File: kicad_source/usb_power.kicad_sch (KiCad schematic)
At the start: 38 parts, among them P1 USB_OTG, Q1 2N7002, Q2 2N7002, Q3 BC847, Q4 BC847, Q5 NTR4171P, SW3 SWITCH_INV, U1 TPS383X, U2 MCP73831, U3 TPS736XX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

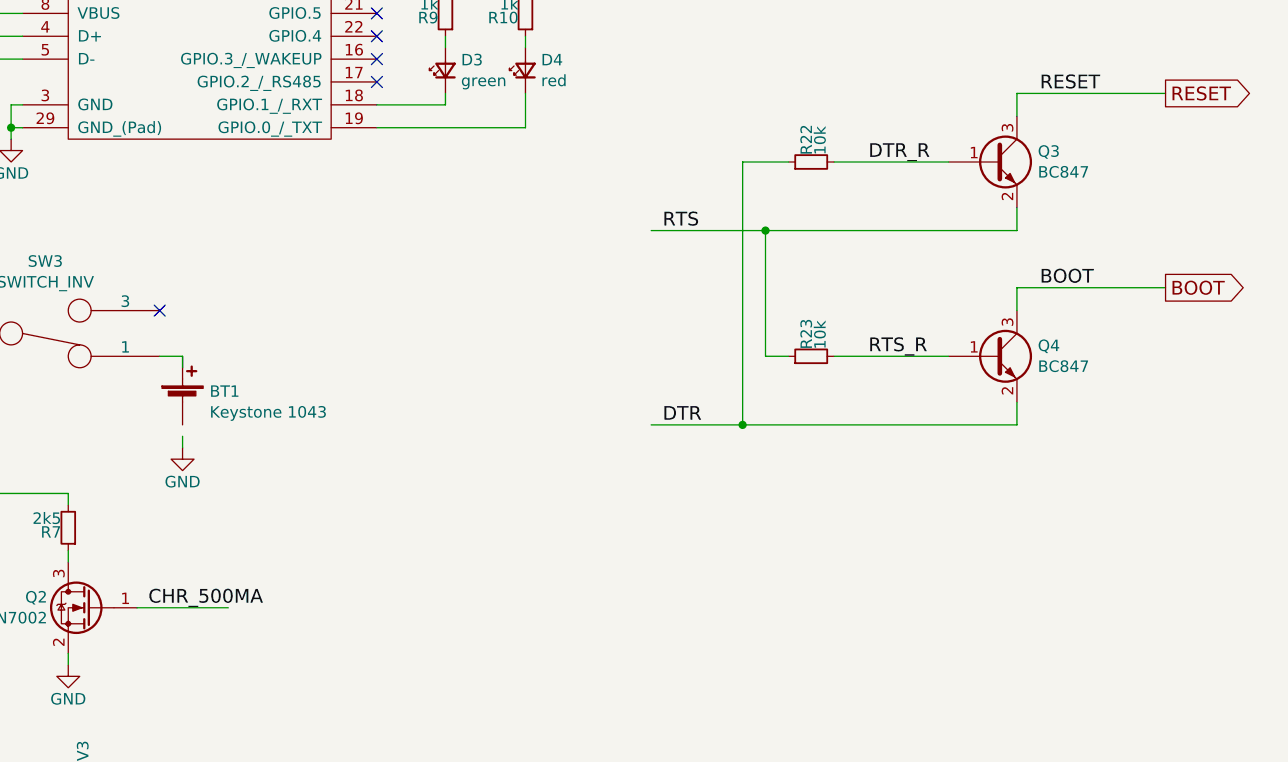
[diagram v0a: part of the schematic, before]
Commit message: added pull up on BOOT
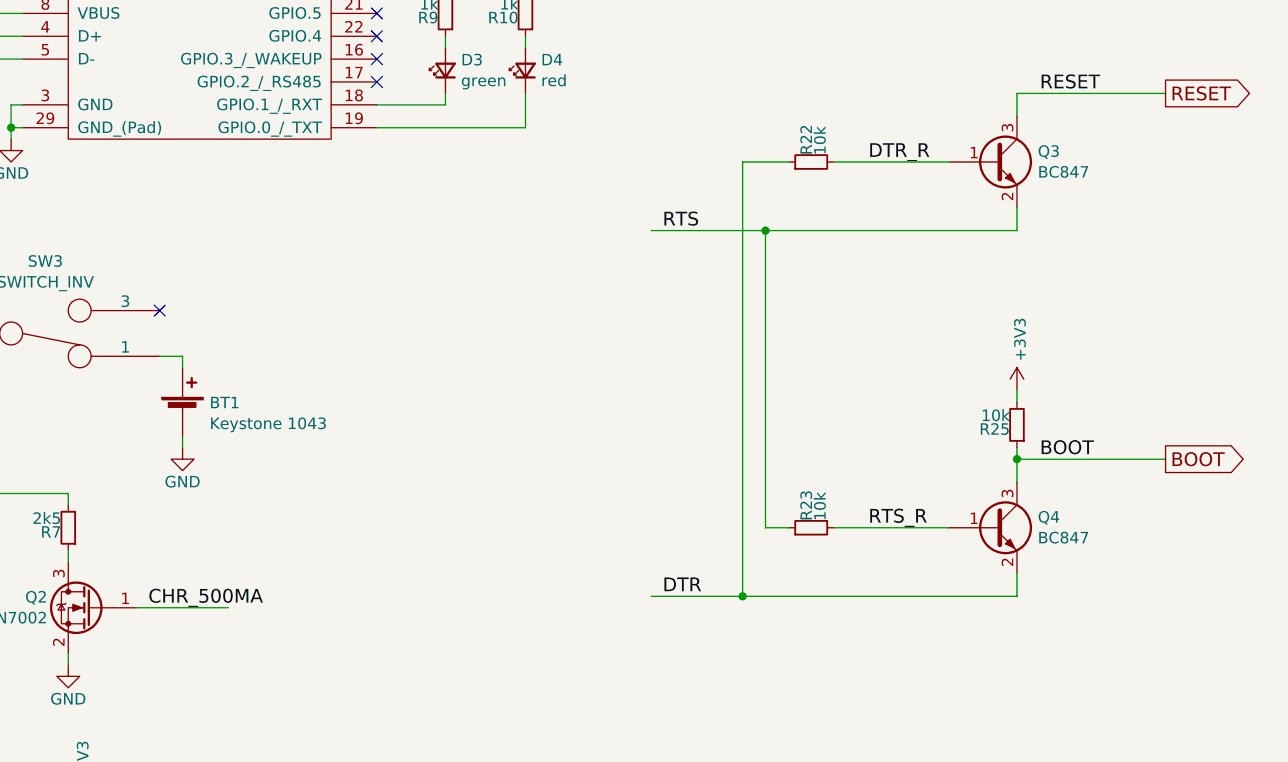
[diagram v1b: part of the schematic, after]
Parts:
- added R25: 10k, Resistor_SMD:R_0603_1608Metric, symbol Device:R_Small
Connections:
- net +3V3: now also R25.2
- net BOOT: now also R25.1
- net GND: now also BT1.2 (-)
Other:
- moved on the sheet: BT1, Q4, R23
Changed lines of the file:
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@@
   (junction (at 110.49 62.23) (diameter 0) (color 0 0 0 0)
   )
+  (junction (at 251.46 121.92) (diameter 0) (color 0 0 0 0)
+  )
   (junction (at 124.46 64.77) (diameter 0) (color 0 0 0 0)
   )
-  (junction (at 220.98 118.11) (diameter 0) (color 0 0 0 0)
+  (junction (at 220.98 137.16) (diameter 0) (color 0 0 0 0)
   )
   (junction (at 116.84 110.49) (diameter 0) (color 0 0 0 0)
@@
     (stroke (width 0) (type default) (color 0 0 0 0))
   )
-  (wire (pts (xy 220.98 118.11) (xy 220.98 88.9))
+  (wire (pts (xy 220.98 88.9) (xy 220.98 137.16))
     (stroke (width 0) (type default) (color 0 0 0 0))
   )
@@
     (stroke (width 0) (type default) (color 0 0 0 0))
   )
-  (wire (pts (xy 223.52 110.49) (xy 226.06 110.49))
+  (wire (pts (xy 223.52 129.54) (xy 226.06 129.54))
     (stroke (width 0) (type default) (color 0 0 0 0))
   )
@@
     (stroke (width 0) (type default) (color 0 0 0 0))
   )
-  (wire (pts (xy 251.46 102.87) (xy 251.46 105.41))
+  (wire (pts (xy 251.46 121.92) (xy 251.46 124.46))
     (stroke (width 0) (type default) (color 0 0 0 0))
   )
@@
     (stroke (width 0) (type default) (color 0 0 0 0))
   )
+  (wire (pts (xy 251.46 114.3) (xy 251.46 115.57))
+    (stroke (width 0) (type default) (color 0 0 0 0))
+  )
   (wire (pts (xy 127 54.61) (xy 140.97 54.61))
     (stroke (width 0) (type default) (color 0 0 0 0))
@@
     (stroke (width 0) (type default) (color 0 0 0 0))
   )
-  (wire (pts (xy 223.52 96.52) (xy 223.52 110.49))
-    (stroke (width 0) (type default) (color 0 0 0 0))
-  )
   (wire (pts (xy 26.67 110.49) (xy 26.67 97.79))
     (stroke (width 0) (type default) (color 0 0 0 0))
@@
     (stroke (width 0) (type default) (color 0 0 0 0))
   )
-  (wire (pts (xy 220.98 118.11) (xy 251.46 118.11))
+  (wire (pts (xy 223.52 96.52) (xy 223.52 129.54))
+    (stroke (width 0) (type default) (color 0 0 0 0))
+  )
+  (wire (pts (xy 220.98 137.16) (xy 251.46 137.16))
     (stroke (width 0) (type default) (color 0 0 0 0))
   )
@@
     (stroke (width 0) (type default) (color 0 0 0 0))
   )
-  (wire (pts (xy 267.97 102.87) (xy 251.46 102.87))
+  (wire (pts (xy 267.97 121.92) (xy 251.46 121.92))
     (stroke (width 0) (type default) (color 0 0 0 0))
   )
@@
     (stroke (width 0) (type default) (color 0 0 0 0))
   )
+  (wire (pts (xy 226.06 88.9) (xy 220.98 88.9))
+    (stroke (width 0) (type default) (color 0 0 0 0))
+  )
   (wire (pts (xy 81.28 46.99) (xy 104.14 46.99))
     (stroke (width 0) (type default) (color 0 0 0 0))
@@
     (stroke (width 0) (type default) (color 0 0 0 0))
   )
-  (wire (pts (xy 231.14 110.49) (xy 243.84 110.49))
+  (wire (pts (xy 231.14 129.54) (xy 243.84 129.54))
     (stroke (width 0) (type default) (color 0 0 0 0))
   )
@@
     (stroke (width 0) (type default) (color 0 0 0 0))
   )
-  (wire (pts (xy 210.82 118.11) (xy 220.98 118.11))
+  (wire (pts (xy 210.82 137.16) (xy 220.98 137.16))
     (stroke (width 0) (type default) (color 0 0 0 0))
   )
@@
     (stroke (width 0) (type default) (color 0 0 0 0))
   )
+  (wire (pts (xy 251.46 120.65) (xy 251.46 121.92))
+    (stroke (width 0) (type default) (color 0 0 0 0))
+  )
   (wire (pts (xy 190.5 59.69) (xy 180.34 59.69))
     (stroke (width 0) (type default) (color 0 0 0 0))
@@
     (stroke (width 0) (type default) (color 0 0 0 0))
   )
-  (wire (pts (xy 220.98 88.9) (xy 226.06 88.9))
-    (stroke (width 0) (type default) (color 0 0 0 0))
-  )
   (wire (pts (xy 64.77 123.19) (xy 64.77 121.92))
     (stroke (width 0) (type default) (color 0 0 0 0))
@@
     (stroke (width 0) (type default) (color 0 0 0 0))
   )
-  (wire (pts (xy 251.46 118.11) (xy 251.46 115.57))
+  (wire (pts (xy 251.46 137.16) (xy 251.46 134.62))
     (stroke (width 0) (type default) (color 0 0 0 0))
   )
@@
     (effects (font (size 1.524 1.524)) (justify left bottom))
   )
-  (label "RTS_R" (at 234.95 110.49 0)
+  (label "RTS_R" (at 234.95 129.54 0)
     (effects (font (size 1.524 1.524)) (justify left bottom))
   )
@@
     (effects (font (size 1.524 1.524)) (justify left bottom))
   )
-  (label "BOOT" (at 254 102.87 0)
+  (label "BOOT" (at 254 121.92 0)
     (effects (font (size 1.524 1.524)) (justify left bottom))
   )
@@
     (effects (font (size 1.524 1.524)) (justify left bottom))
   )
-  (label "DTR" (at 212.09 118.11 0)
+  (label "DTR" (at 212.09 137.16 0)
     (effects (font (size 1.524 1.524)) (justify left bottom))
   )
@@
     (effects (font (size 1.524 1.524)) (justify left bottom))
   )
-  (global_label "BOOT" (shape output) (at 267.97 102.87 0) (fields_autoplaced)
+  (global_label "BOOT" (shape output) (at 267.97 121.92 0) (fields_autoplaced)
     (effects (font (size 1.524 1.524)) (justify left))
-    (property "Referenzen zwischen Schaltplänen" "${INTERSHEET_REFS}" (id 0) (at 0 0 0)
+    (property "Referenzen zwischen Schaltplänen" "${INTERSHEET_REFS}" (id 0) (at 0 19.05 0)
       (effects (font (size 1.27 1.27)) hide)
     )
@@
     (pin "1")
   )
-  (symbol (lib_id "Device:Battery_Cell") (at 158.75 115.57 0) (unit 1)
-    (in_bom yes) (on_board yes)
-    (property "Reference" "BT1" (id 0) (at 161.7472 114.4016 0)
-      (effects (font (size 1.27 1.27)) (justify left))
-    )
-    (property "Value" "Keystone 1043" (id 1) (at 161.7472 116.713 0)
-      (effects (font (size 1.27 1.27)) (justify left))
-    )
-    (property "Footprint" "MECH_battery_holder:KEYSTONE_1043" (id 2) (at 158.75 114.554 90)
-      (effects (font (size 1.27 1.27)) hide)
-    )
-    (property "Datasheet" "" (id 3) (at 158.75 114.554 90))
+  (symbol (lib_id "Device:Battery_Cell") (at 158.75 116.84 0) (unit 1)
+    (in_bom yes) (on_board yes)
+    (property "Reference" "BT1" (id 0) (at 161.7472 115.6716 0)
+      (effects (font (size 1.27 1.27)) (justify left))
+    )
+    (property "Value" "Keystone 1043" (id 1) (at 161.7472 117.983 0)
+      (effects (font (size 1.27 1.27)) (justify left))
+    )
+    (property "Footprint" "MECH_battery_holder:KEYSTONE_1043" (id 2) (at 158.75 115.824 90)
+      (effects (font (size 1.27 1.27)) hide)
+    )
+    (property "Datasheet" "" (id 3) (at 158.75 115.824 90))
     (pin "1")
     (pin "2")
@@
     (pin "2")
   )
-  (symbol (lib_id "Device:Q_NPN_BEC") (at 248.92 110.49 0) (unit 1)
-    (in_bom yes) (on_board yes)
-    (property "Reference" "Q4" (id 0) (at 253.7714 109.3216 0)
-      (effects (font (size 1.27 1.27)) (justify left))
-    )
-    (property "Value" "BC847" (id 1) (at 253.7714 111.633 0)
-      (effects (font (size 1.27 1.27)) (justify left))
-    )
-    (property "Footprint" "SOT_TO:SOT-23" (id 2) (at 254 107.95 0)
-      (effects (font (size 1.27 1.27)) hide)
-    )
-    (property "Datasheet" "" (id 3) (at 248.92 110.49 0))
+  (symbol (lib_id "Device:Q_NPN_BEC") (at 248.92 129.54 0) (unit 1)
+    (in_bom yes) (on_board yes)
+    (property "Reference" "Q4" (id 0) (at 253.7714 128.3716 0)
+      (effects (font (size 1.27 1.27)) (justify left))
+    )
+    (property "Value" "BC847" (id 1) (at 253.7714 130.683 0)
+      (effects (font (size 1.27 1.27)) (justify left))
+    )
+    (property "Footprint" "SOT_TO:SOT-23" (id 2) (at 254 127 0)
+      (effects (font (size 1.27 1.27)) hide)
+    )
+    (property "Datasheet" "" (id 3) (at 248.92 129.54 0))
     (pin "1")
     (pin "2")
     (pin "3")
   )
-  (symbol (lib_id "Device:R_Small") (at 228.6 110.49 90) (unit 1)
-    (in_bom yes) (on_board yes)
-    (property "Reference" "R23" (id 0) (at 228.092 109.728 0)
-      (effects (font (size 1.27 1.27)) (justify left))
-    )
-    (property "Value" "10k" (id 1) (at 229.616 109.728 0)
-      (effects (font (size 1.27 1.27)) (justify left))
-    )
-    (property "Footprint" "resistors:R_0603" (id 2) (at 232.41 110.49 0)
-      (effects (font (size 1.27 1.27)) hide)
-    )
-    (property "Datasheet" "" (id 3) (at 228.6 110.49 0))
+  (symbol (lib_id "Device:R_Small") (at 228.6 129.54 90) (unit 1)
+    (in_bom yes) (on_board yes)
+    (property "Reference" "R23" (id 0) (at 228.092 128.778 0)
+      (effects (font (size 1.27 1.27)) (justify left))
+    )
+    (property "Value" "10k" (id 1) (at 229.616 128.778 0)
+      (effects (font (size 1.27 1.27)) (justify left))
+    )
+    (property "Footprint" "resistors:R_0603" (id 2) (at 232.41 129.54 0)
+      (effects (font (size 1.27 1.27)) hide)
+    )
+    (property "Datasheet" "" (id 3) (at 228.6 129.54 0))
     (pin "1")
     (pin "2")
@@
     (pin "2")
   )
+  (symbol (lib_id "Device:R_Small") (at 251.46 118.11 180) (unit 1)
+    (in_bom yes) (on_board yes)
+    (property "Reference" "R25" (id 0) (at 250.698 118.618 0)
+      (effects (font (size 1.27 1.27)) (justify left))
+    )
+    (property "Value" "10k" (id 1) (at 250.698 117.094 0)
+      (effects (font (size 1.27 1.27)) (justify left))
+    )
+    (property "Footprint" "Resistor_SMD:R_0603_1608Metric" (id 2) (at 251.46 114.3 0)
+      (effects (font (size 1.27 1.27)) hide)
+    )
+    (property "Datasheet" "" (id 3) (at 251.46 118.11 0))
+    (pin "1")
+    (pin "2")
+  )
+  (symbol (lib_id "power:+3V3") (at 251.46 114.3 0) (unit 1)
+    (in_bom yes) (on_board yes)
+    (property "Reference" "#PWR010" (id 0) (at 251.46 118.11 0)
+      (effects (font (size 1.27 1.27)) hide)
+    )
+    (property "Value" "+3V3" (id 1) (at 251.841 111.0488 90)
+      (effects (font (size 1.27 1.27)) (justify left))
+    )
+    (property "Footprint" "" (id 2) (at 251.46 114.3 0))
+    (property "Datasheet" "" (id 3) (at 251.46 114.3 0))
+    (pin "1")
+  )
 )
